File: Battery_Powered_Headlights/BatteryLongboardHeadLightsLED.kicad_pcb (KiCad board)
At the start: 2 copper layers, 2 parts

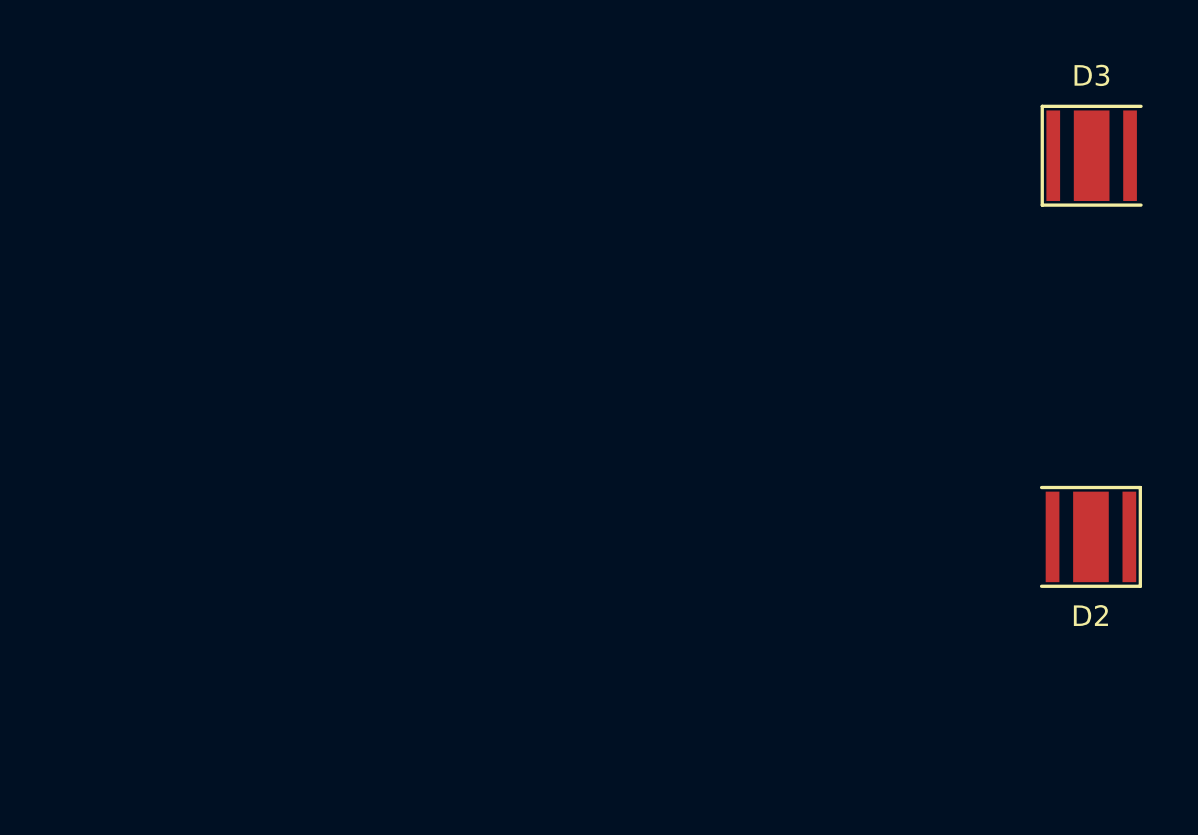
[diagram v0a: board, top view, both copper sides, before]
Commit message: PCB's should now be orderable
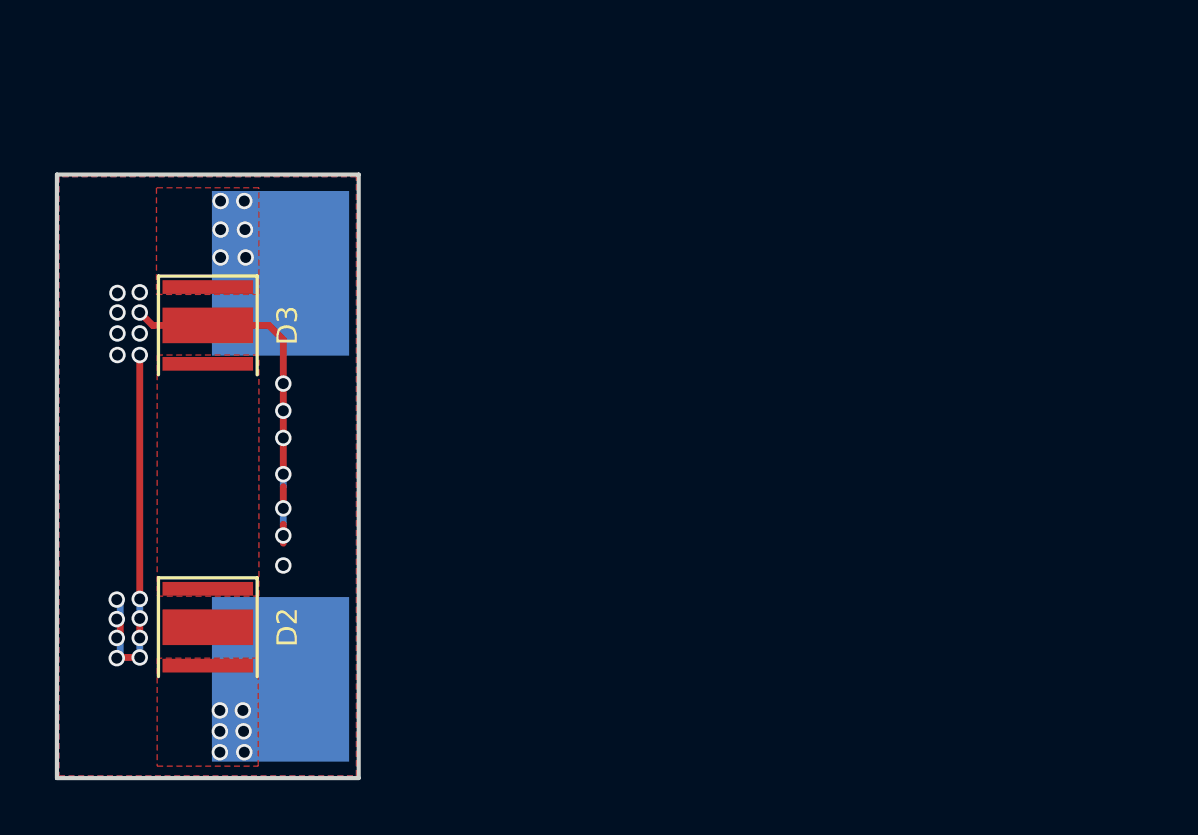
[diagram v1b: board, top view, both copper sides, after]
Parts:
- added J2: Conn_01x01, Global_Parts:SolderWirePad_single_SMD_5x6mm, B.Cu at (162.9, 105.3)
- added J3: Conn_01x01, Global_Parts:SolderWirePad_single_SMD_5x6mm, B.Cu at (162.9, 90.5)
- moved D3 32.8 mm to (160.2, 92.4), turned to 270 degrees
- moved D2 32.4 mm to (160.2, 103.4), turned to 270 degrees
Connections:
- D2 pad 3: (no net) -> GND
- D3 pad 3: (no net) -> GND
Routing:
- net GND: track 0.00 -> 27.2 mm, vias 0 -> 23
- net Net-(D3-Pad1): vias 0 -> 6
- net Net-(C4-Pad1): vias 0 -> 6
- added copper zone on B.Cu, net GND
- added copper zone on F.Cu, net GND
- added copper zone on F.Cu, net Net-(C4-Pad1)
- added copper zone on F.Cu, net Net-(D2-Pad1)
- added copper zone on F.Cu, net Net-(D3-Pad1)
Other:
- board outline added: 11 x 22 mm
